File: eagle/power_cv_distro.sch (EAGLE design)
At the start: 11 parts, among them U1 POWER, U2 POWER, U3 POWER, U4 POWER, U5 POWER, U6 POWER, U7 POWER, U8 POWER, U9 POWER

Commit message: opamps
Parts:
- added R1, R2, R5, R6: 1k8, rcl:R-US_0204/2V
- added R3, R4, R8, R9: 1k, rcl:R-US_0207/7
- added U10, U11, U12, U13: TLV2372IP, Texas Instruments_By_element14_Batch_1:TLV2372IP
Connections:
- new net N$17: R1.2, U10.2OUT, U6.CV
- new net N$18: R2.2, U10.1OUT, U5.CV
- new net N$19: R1.1, R3.2, U10.2IN-
- new net N$20: R2.1, R4.2, U10.1IN-
- new net N$22: R6.2, U11.2OUT, U2.CV
- new net N$23: R5.1, R9.2, U11.1IN-
- new net N$24: R6.1, R8.2, U11.2IN-
- new net N$26: R5.2, U1.CV, U11.1OUT
- net +12V: now also U10.VDD, U11.VDD
- net GND: now also R3.1, R4.1, R8.1, R9.1, U10.GND, U11.GND
- net N$2: now also U10.1IN_+; no longer U5.CV
- net N$4: now also U10.2IN+; no longer U6.CV
- net N$6: now also U11.1IN_+; no longer U1.CV
- net N$8: now also U11.2IN+; no longer U2.CV
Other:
- moved on the sheet: JP2, JP3, U9

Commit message: opamps in
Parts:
- added R10, R13, R14, R7: 1k8, rcl:R-US_0204/2V
- added R11, R12, R15, R16: 1k, rcl:R-US_0207/7
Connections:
- new net N$21: R11.2, R7.1, U12.1IN-
- new net N$25: R10.1, R12.2, U12.2IN-
- new net N$27: R7.2, U12.1OUT, U3.CV
- new net N$28: R13.2, U13.1OUT, U4.CV
- new net N$29: R14.2, U13.2OUT, U8.CV
- new net N$30: JP3.3, U13.1IN_+
- new net N$31: R13.1, R15.2, U13.1IN-
- new net N$32: R14.1, R16.2, U13.2IN-
- net +12V: now also U12.VDD, U13.VDD
- net GND: now also R11.1, R12.1, R15.1, R16.1, U12.GND, U13.GND
- net N$10: now also U12.1IN_+; no longer U3.CV
- net N$12: now also U12.2IN+; no longer U7.CV
- net N$14: now also R10.2, U12.2OUT, U7.CV; no longer JP3.3, U4.CV
- net N$16: now also U13.2IN+; no longer U8.CV
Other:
- moved on the sheet: JP3, U12, U13

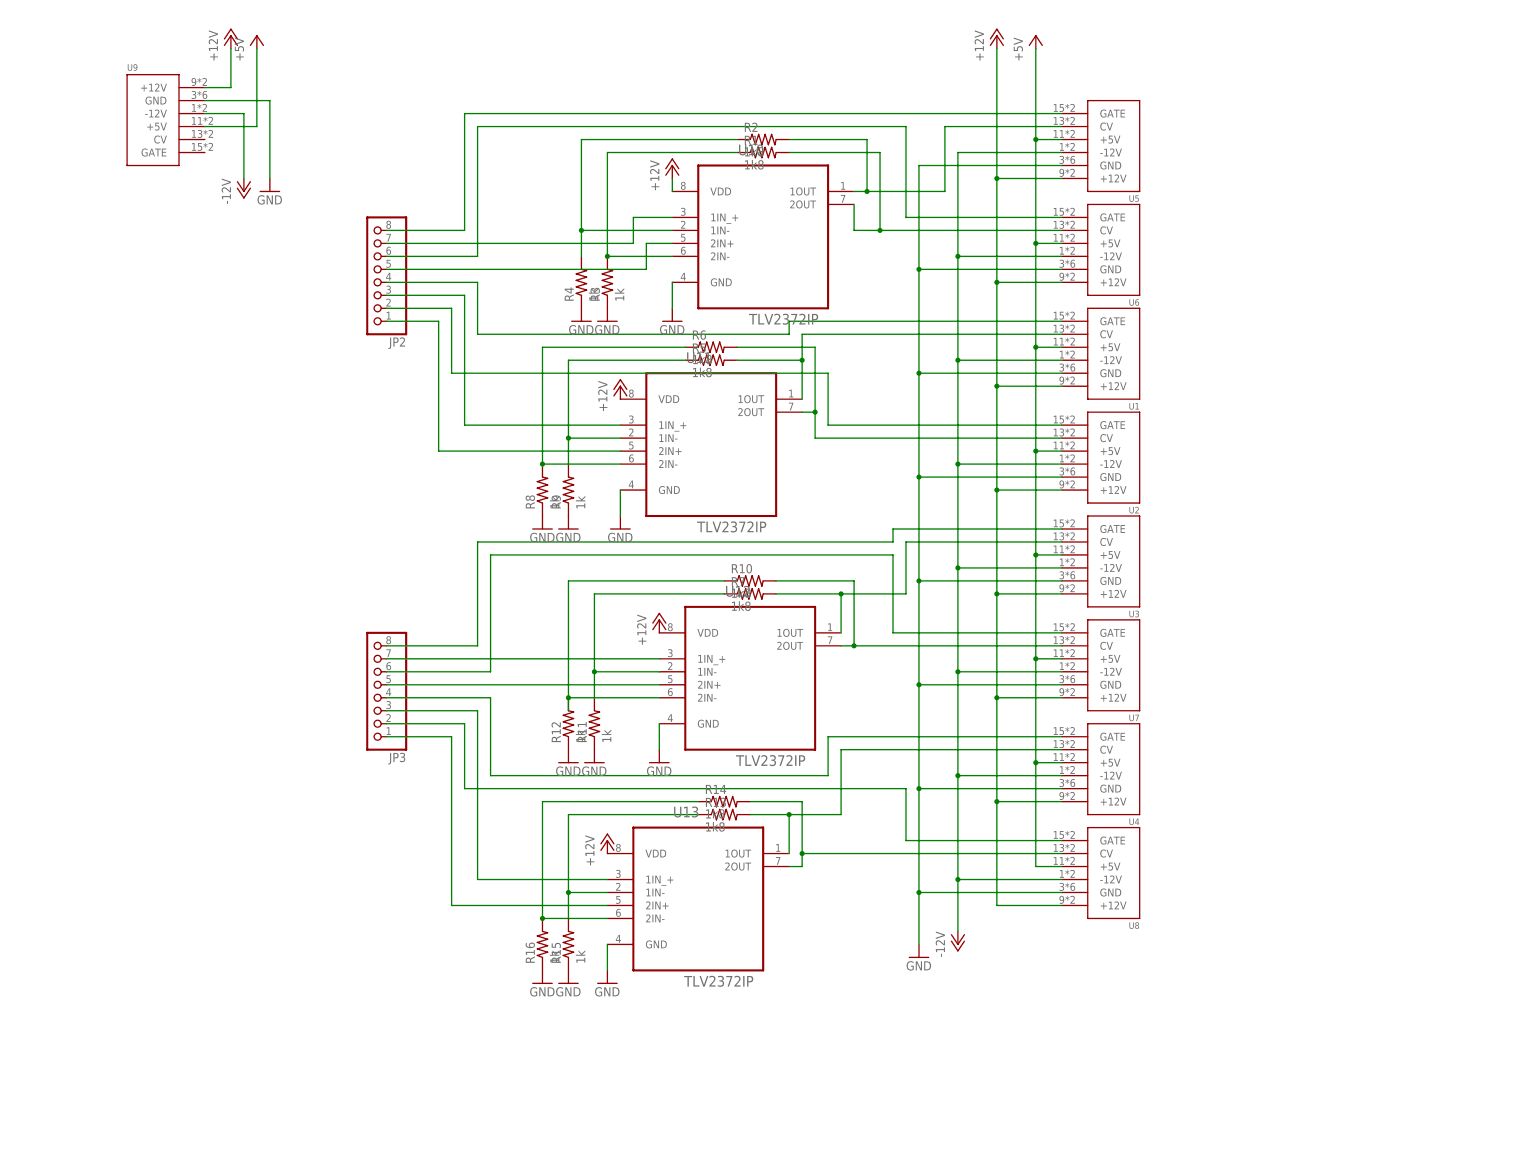
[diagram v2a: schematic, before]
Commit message: output resistors
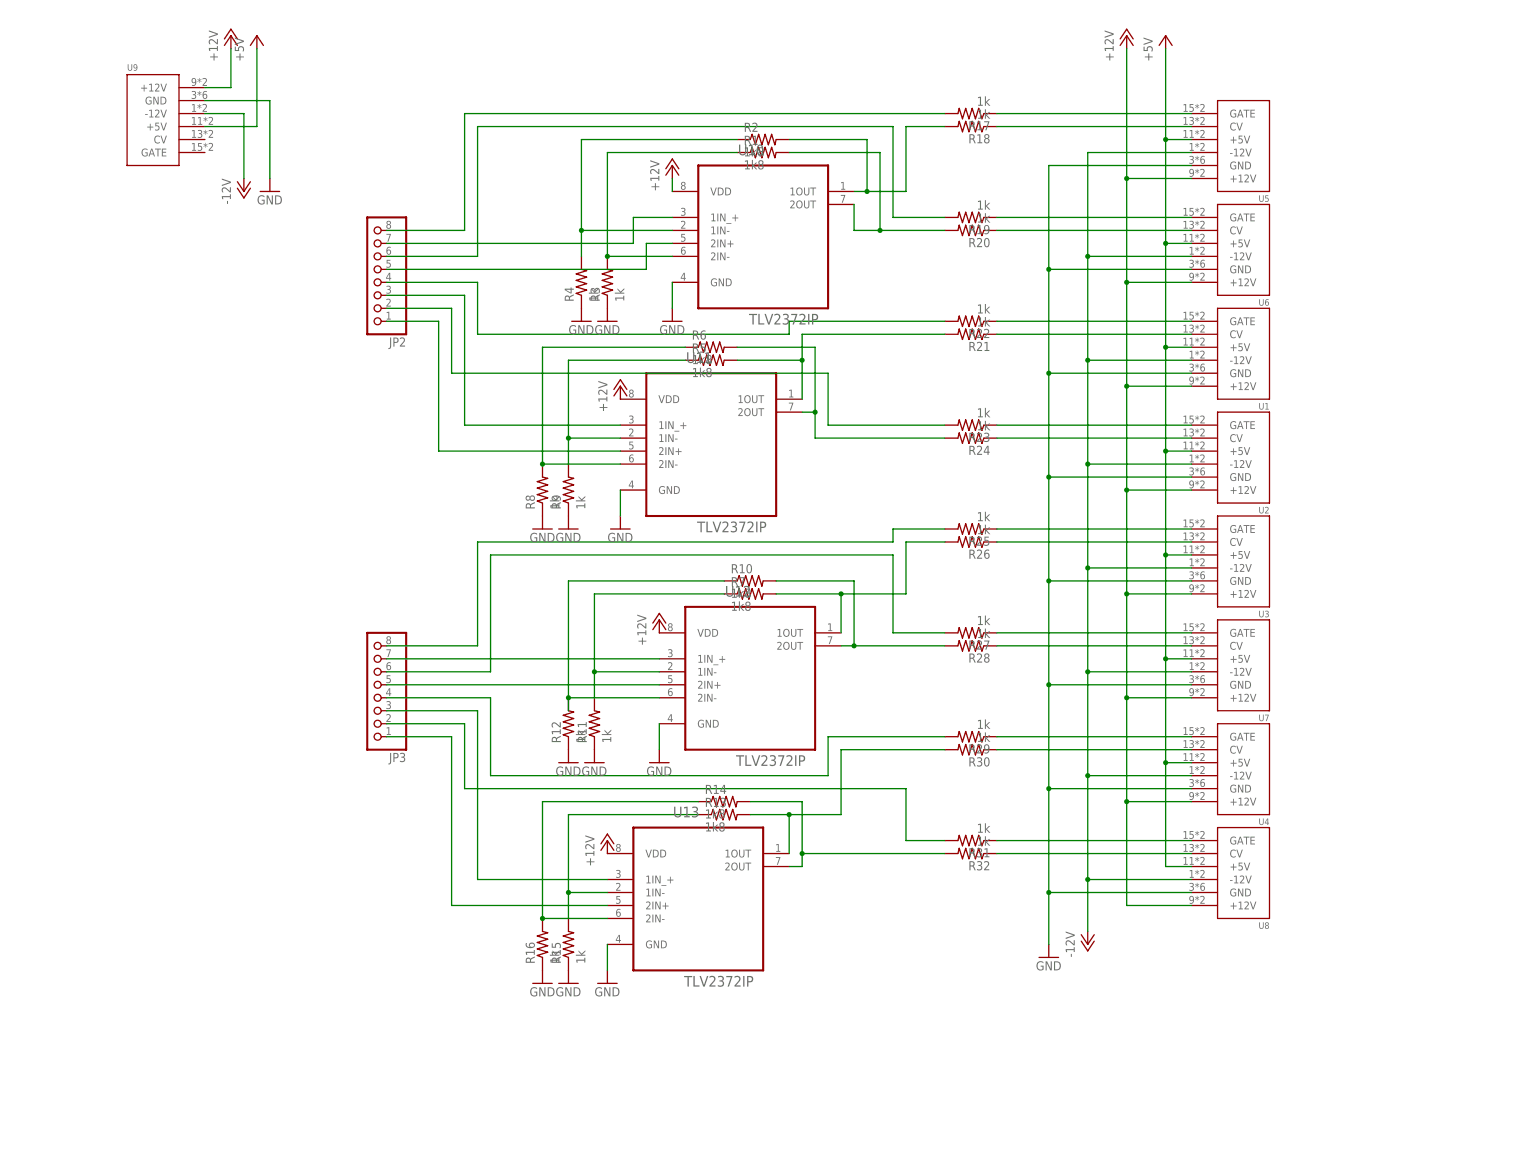
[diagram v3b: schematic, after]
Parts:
- added R17, R18, R19, R20, R21, R22, R23, R24, R25, R26, R27, R28, R29, R30, R31, R32: 1k, rcl:R-US_0207/7
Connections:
- new net N$33: R17.1, U5.GATE
- new net N$34: R18.1, U5.CV
- new net N$35: R20.1, U6.CV
- new net N$36: R19.1, U6.GATE
- new net N$37: R22.1, U1.GATE
- new net N$38: R21.1, U1.CV
- new net N$39: R23.1, U2.GATE
- new net N$40: R24.1, U2.CV
- new net N$41: R25.1, U3.GATE
- new net N$42: R26.1, U3.CV
- new net N$43: R27.1, U7.GATE
- new net N$44: R28.1, U7.CV
- new net N$45: R29.1, U4.GATE
- new net N$46: R30.1, U4.CV
- new net N$47: R31.1, U8.GATE
- new net N$48: R32.1, U8.CV
- net N$1: now also R17.2; no longer U5.GATE
- net N$11: now also R27.2; no longer U7.GATE
- net N$13: now also R29.2; no longer U4.GATE
- net N$14: now also R28.2; no longer U7.CV
- net N$15: now also R31.2; no longer U8.GATE
- net N$17: now also R20.2; no longer U6.CV
- net N$18: now also R18.2; no longer U5.CV
- net N$22: now also R24.2; no longer U2.CV
- net N$26: now also R21.2; no longer U1.CV
- net N$27: now also R26.2; no longer U3.CV
- net N$28: now also R30.2; no longer U4.CV
- net N$29: now also R32.2; no longer U8.CV
- net N$3: now also R19.2; no longer U6.GATE
- net N$5: now also R22.2; no longer U1.GATE
- net N$7: now also R23.2; no longer U2.GATE
- net N$9: now also R25.2; no longer U3.GATE
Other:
- moved on the sheet: U1, U2, U3, U4, U5, U6, U7, U8

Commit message: route tweaked
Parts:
- added C1, C2, C3, C4: (no value), rcl:C-US025-025X050
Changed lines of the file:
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@@
 <part name="R31" library="rcl" deviceset="R-US_" device="0207/7" value="1k"/>
 <part name="R32" library="rcl" deviceset="R-US_" device="0207/7" value="1k"/>
+<part name="C1" library="rcl" deviceset="C-US" device="025-025X050"/>
+<part name="C2" library="rcl" deviceset="C-US" device="025-025X050"/>
+<part name="C3" library="rcl" deviceset="C-US" device="025-025X050"/>
+<part name="C4" library="rcl" deviceset="C-US" device="025-025X050"/>
 </parts>
 <sheets>
@@
 <instance part="R31" gate="G$1" x="91.44" y="-40.64" rot="R180"/>
 <instance part="R32" gate="G$1" x="91.44" y="-43.18" rot="R180"/>
+<instance part="C1" gate="G$1" x="-38.1" y="106.68"/>
+<instance part="C2" gate="G$1" x="-30.48" y="106.68"/>
+<instance part="C3" gate="G$1" x="-22.86" y="106.68"/>
+<instance part="C4" gate="G$1" x="-15.24" y="106.68"/>
 </instances>
 <busses>

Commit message: cutout
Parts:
- C1, C2, C3, C4: value (none) -> 100n
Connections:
- net +12V: now also C1.1, C2.1, C3.1, C4.1
- net GND: now also C1.2, C2.2, C3.2, C4.2
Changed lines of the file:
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@@
 <?xml version="1.0" encoding="utf-8"?>
 <!DOCTYPE eagle SYSTEM "eagle.dtd">
-<eagle version="7.2.0">
+<eagle version="7.1.0">
 <drawing>
 <settings>
@@
 <part name="R31" library="rcl" deviceset="R-US_" device="0207/7" value="1k"/>
 <part name="R32" library="rcl" deviceset="R-US_" device="0207/7" value="1k"/>
-<part name="C1" library="rcl" deviceset="C-US" device="025-025X050"/>
-<part name="C2" library="rcl" deviceset="C-US" device="025-025X050"/>
-<part name="C3" library="rcl" deviceset="C-US" device="025-025X050"/>
-<part name="C4" library="rcl" deviceset="C-US" device="025-025X050"/>
+<part name="C1" library="rcl" deviceset="C-US" device="025-025X050" value="100n"/>
+<part name="C2" library="rcl" deviceset="C-US" device="025-025X050" value="100n"/>
+<part name="C3" library="rcl" deviceset="C-US" device="025-025X050" value="100n"/>
+<part name="C4" library="rcl" deviceset="C-US" device="025-025X050" value="100n"/>
 </parts>
 <sheets>
@@
 <pinref part="GND2" gate="1" pin="GND"/>
 <wire x1="-58.42" y1="104.14" x2="-45.72" y2="104.14" width="0.1524" layer="91"/>
-<wire x1="-45.72" y1="104.14" x2="-45.72" y2="88.9" width="0.1524" layer="91"/>
+<wire x1="-45.72" y1="104.14" x2="-45.72" y2="99.06" width="0.1524" layer="91"/>
+<pinref part="C4" gate="G$1" pin="2"/>
+<wire x1="-45.72" y1="99.06" x2="-45.72" y2="88.9" width="0.1524" layer="91"/>
+<wire x1="-45.72" y1="99.06" x2="-38.1" y2="99.06" width="0.1524" layer="91"/>
+<wire x1="-38.1" y1="99.06" x2="-30.48" y2="99.06" width="0.1524" layer="91"/>
+<wire x1="-30.48" y1="99.06" x2="-22.86" y2="99.06" width="0.1524" layer="91"/>
+<wire x1="-22.86" y1="99.06" x2="-15.24" y2="99.06" width="0.1524" layer="91"/>
+<wire x1="-15.24" y1="99.06" x2="-15.24" y2="101.6" width="0.1524" layer="91"/>
+<junction x="-45.72" y="99.06"/>
+<pinref part="C3" gate="G$1" pin="2"/>
+<wire x1="-22.86" y1="101.6" x2="-22.86" y2="99.06" width="0.1524" layer="91"/>
+<junction x="-22.86" y="99.06"/>
+<pinref part="C2" gate="G$1" pin="2"/>
+<wire x1="-30.48" y1="101.6" x2="-30.48" y2="99.06" width="0.1524" layer="91"/>
+<junction x="-30.48" y="99.06"/>
+<pinref part="C1" gate="G$1" pin="2"/>
+<wire x1="-38.1" y1="101.6" x2="-38.1" y2="99.06" width="0.1524" layer="91"/>
+<junction x="-38.1" y="99.06"/>
 </segment>
 <segment>
@@
 <pinref part="P+3" gate="1" pin="+12V"/>
 <wire x1="-58.42" y1="106.68" x2="-53.34" y2="106.68" width="0.1524" layer="91"/>
-<wire x1="-53.34" y1="106.68" x2="-53.34" y2="114.3" width="0.1524" layer="91"/>
-</segment>
-<segment>
+<wire x1="-53.34" y1="106.68" x2="-53.34" y2="111.76" width="0.1524" layer="91"/>
+<pinref part="C4" gate="G$1" pin="1"/>
+<wire x1="-53.34" y1="111.76" x2="-53.34" y2="114.3" width="0.1524" layer="91"/>
+<wire x1="-53.34" y1="111.76" x2="-38.1" y2="111.76" width="0.1524" layer="91"/>
+<wire x1="-38.1" y1="111.76" x2="-30.48" y2="111.76" width="0.1524" layer="91"/>
+<wire x1="-30.48" y1="111.76" x2="-22.86" y2="111.76" width="0.1524" layer="91"/>
+<wire x1="-22.86" y1="111.76" x2="-15.24" y2="111.76" width="0.1524" layer="91"/>
+<wire x1="-15.24" y1="111.76" x2="-15.24" y2="109.22" width="0.1524" layer="91"/>
+<junction x="-53.34" y="111.76"/>
+<pinref part="C3" gate="G$1" pin="1"/>
+<wire x1="-22.86" y1="109.22" x2="-22.86" y2="111.76" width="0.1524" layer="91"/>
+<junction x="-22.86" y="111.76"/>
+<pinref part="C2" gate="G$1" pin="1"/>
+<wire x1="-30.48" y1="109.22" x2="-30.48" y2="111.76" width="0.1524" layer="91"/>
+<junction x="-30.48" y="111.76"/>
+<pinref part="C1" gate="G$1" pin="1"/>
+<wire x1="-38.1" y1="109.22" x2="-38.1" y2="111.76" width="0.1524" layer="91"/>
+<junction x="-38.1" y="111.76"/>
+</segment>
+<segment>

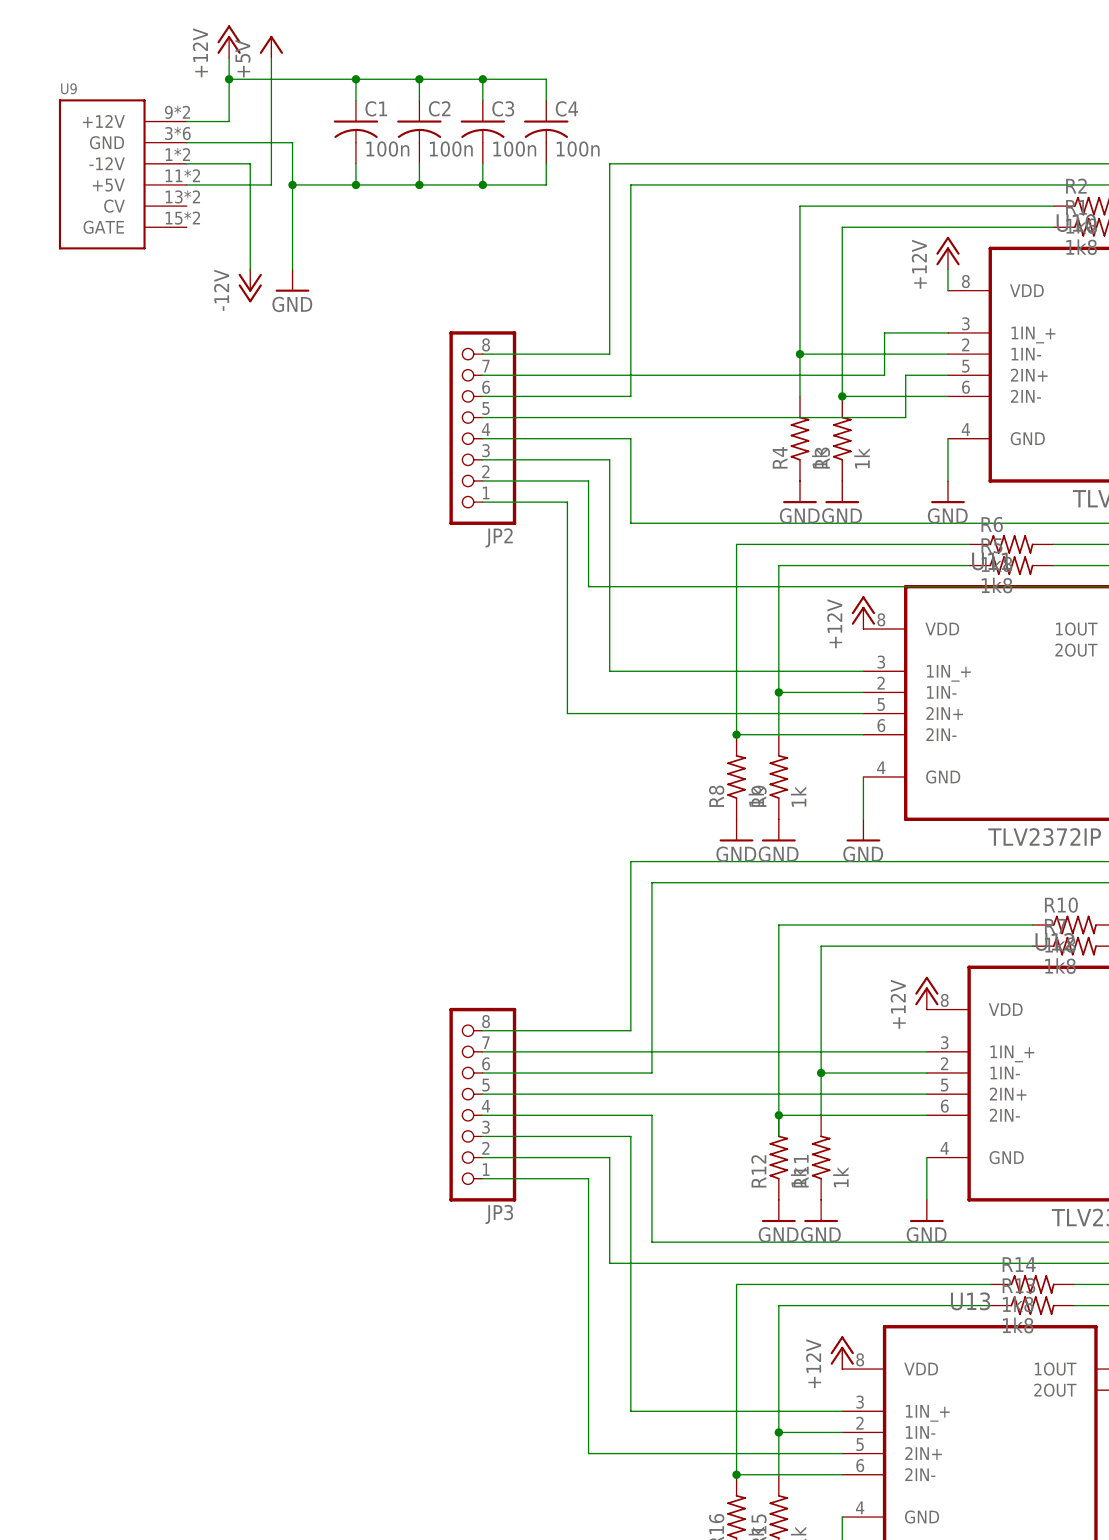
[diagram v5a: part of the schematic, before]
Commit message: filtering power for scale opamps
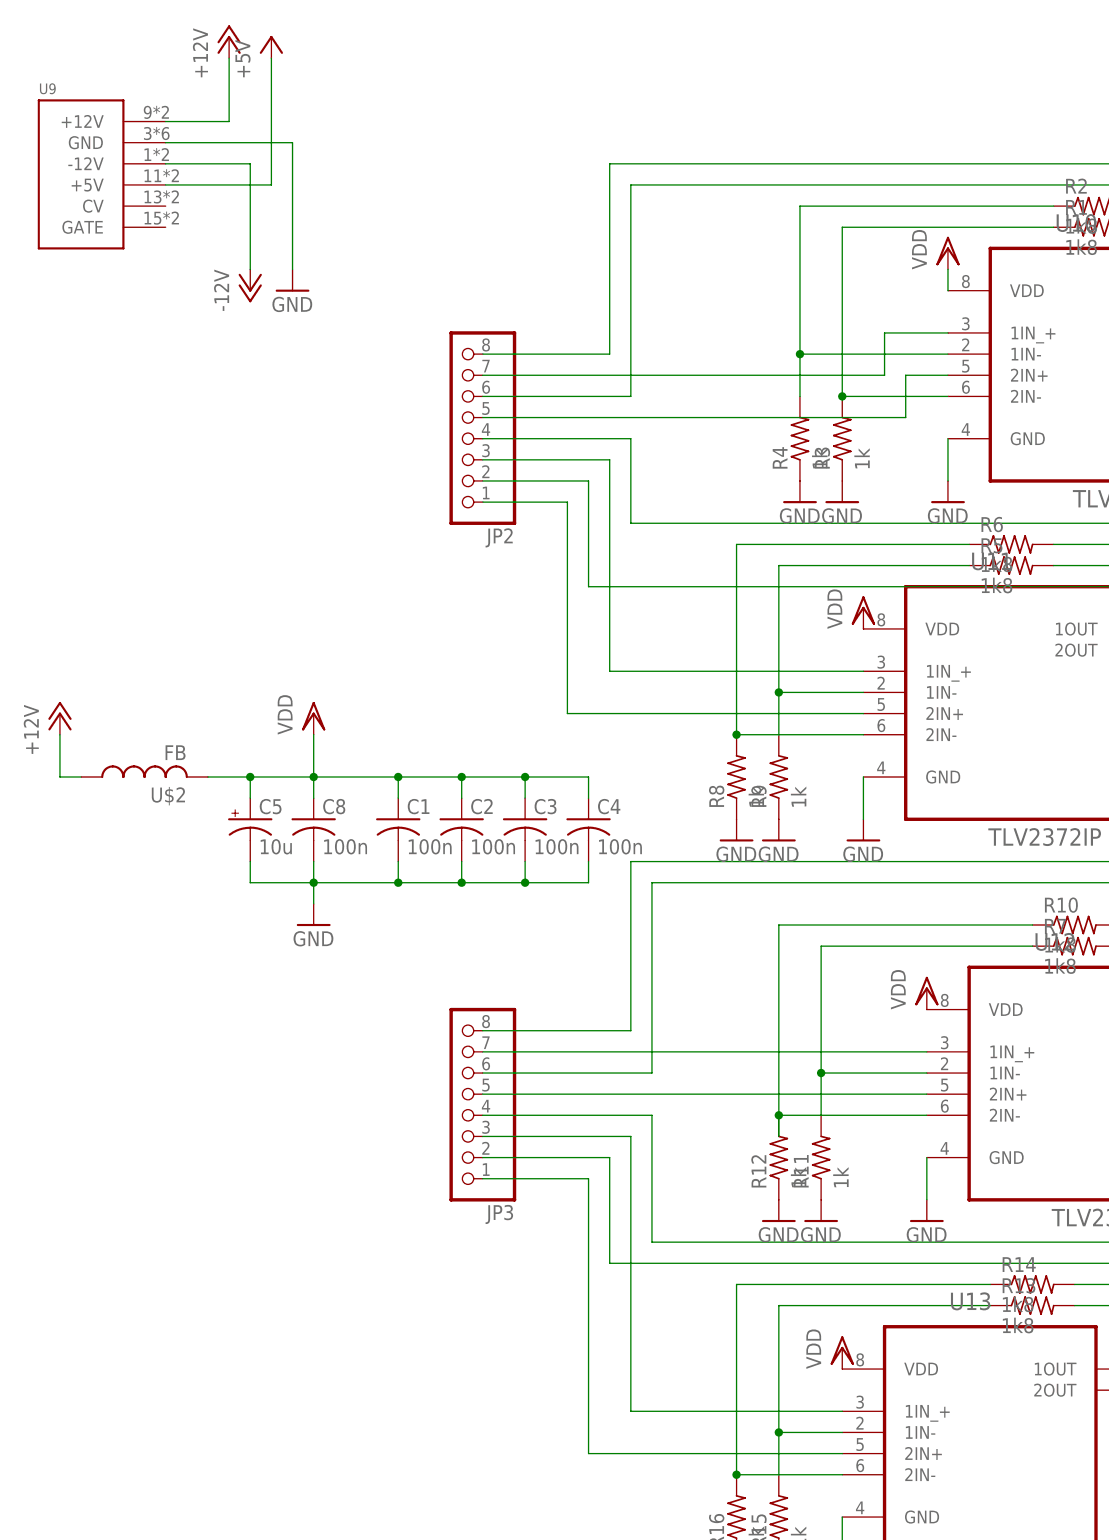
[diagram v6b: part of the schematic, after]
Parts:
- added C5: 10u, rcl:CPOL-USB45181A
- added C8: 100n, rcl:C-US050-024X044
- added U$2: FB, adafruit:FB
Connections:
- new net N$49: U1.+12V, U2.+12V, U3.+12V, U4.+12V, U5.+12V, U6.+12V, U7.+12V, U8.+12V
- new net VDD: C1.1, C2.1, C3.1, C4.1, C5.+, C8.1, U$2.2, U10.VDD, U11.VDD, U12.VDD, U13.VDD
- net +12V: now also U$2.1; no longer C1.1, C2.1, C3.1, C4.1, U1.+12V, U10.VDD, U11.VDD, U12.VDD, U13.VDD, U2.+12V, U3.+12V, U4.+12V, U5.+12V, U6.+12V, U7.+12V, U8.+12V
- net GND: now also C5.-, C8.2
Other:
- moved on the sheet: C1, C2, C3, C4, U9
